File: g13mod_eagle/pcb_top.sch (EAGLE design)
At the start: 4 parts

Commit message: wiring
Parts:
- added CN6: (no value), pinhead-half-pitch:THROUHOLE18
- added CN7: (no value), pinhead-half-pitch:THROUHOLE15
- added JP2, JP3: (no value), pinhead-half-pitch:THROUHOLE05
- added JP4, JP7: (no value), pinhead-half-pitch:THROUHOLE04
- added JP5, JP6: (no value), pinhead-half-pitch:THROUHOLE12
- added LED1, LED2, LED3, LED4: (no value), led:LEDCHIPLED_1206
- added R1, R2, R3, R4: (no value), rcl:R-US_R0603
- renumbered S1 to M1, S2 to M2, S3 to M3, S4 to MR
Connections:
- new net CN6_1: CN6.1, M3.S1
- new net CN6_10: CN6.10, JP5.5
- new net CN6_11: CN6.11, JP5.6
- new net CN6_12: CN6.12, M1.S1
- new net CN6_13: CN6.13, JP5.7
- new net CN6_14: CN6.14, JP5.8
- new net CN6_15: CN6.15, JP5.9, M2.S1
- new net CN6_16: CN6.16, JP5.10
- new net CN6_17: CN6.17, JP5.11
- new net CN6_18: CN6.18, JP5.12
- new net CN6_2: CN6.2, MR.S1
- new net CN6_3: CN6.3, JP6.10
- new net CN6_4: CN6.4, JP6.11
- new net CN6_5: CN6.5, JP6.12
- new net CN6_6: CN6.6, JP5.1
- new net CN6_7: CN6.7, JP5.2
- new net CN6_8: CN6.8, JP5.3
- new net CN6_9: CN6.9, JP5.4
- new net CN7_1: CN7.1, JP2.1
- new net CN7_10: CN7.10, JP6.4
- new net CN7_11: CN7.11, JP6.5
- new net CN7_12: CN7.12, JP6.6
- new net CN7_13: CN7.13, JP6.7
- new net CN7_14: CN7.14, JP6.8
- new net CN7_15: CN7.15, JP6.9
- new net CN7_2: CN7.2, JP2.2
- new net CN7_3: CN7.3, JP2.3
- new net CN7_4: CN7.4, JP2.4
- new net CN7_5: CN7.5, M1.P1, M2.P1, MR.P1
- new net CN7_6: CN7.6, JP2.5
- new net CN7_7: CN7.7, JP6.1, M3.P1
- new net CN7_8: CN7.8, JP6.2
- new net CN7_9: CN7.9, JP6.3
- new net LED_M1: JP3.4, R1.1
- new net LED_M2: JP3.3, R2.1
- new net LED_M3: JP3.2, R3.1
- new net LED_MR: JP3.1, R4.1
- new net N$1: JP4.1, JP7.1
- new net N$2: JP4.2, JP7.2
- new net N$3: JP4.3, JP7.3
- new net N$4: JP4.4, JP7.4
- new net N$5: JP3.5, LED1.A, LED2.A, LED3.A, LED4.A
- new net N$6: LED1.C, R1.2
- new net N$7: LED2.C, R2.2
- new net N$8: LED3.C, R3.2
- new net N$9: LED4.C, R4.2

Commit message: wiring top pcb
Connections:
- net CN6_15: no longer JP5.9
- net CN6_16: now also JP5.9; no longer JP5.10
- net CN6_17: now also JP5.10; no longer JP5.11
- net CN6_18: now also JP5.11; no longer JP5.12
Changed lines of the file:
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@@
 </segment>
 <segment>
-<pinref part="JP5" gate="G$1" pin="12"/>
-<wire x1="-2.54" y1="0" x2="-2.54" y2="-5.08" width="0.1524" layer="91"/>
-<label x="-2.54" y="-5.08" size="1.778" layer="95" rot="R270" xref="yes"/>
+<label x="0" y="-5.08" size="1.778" layer="95" rot="R270" xref="yes"/>
+<pinref part="JP5" gate="G$1" pin="11"/>
+<wire x1="0" y1="0" x2="0" y2="-5.08" width="0.1524" layer="91"/>
 </segment>
 </net>
@@
 </segment>
 <segment>
-<label x="0" y="-5.08" size="1.778" layer="95" rot="R270" xref="yes"/>
-<pinref part="JP5" gate="G$1" pin="11"/>
-<wire x1="0" y1="0" x2="0" y2="-5.08" width="0.1524" layer="91"/>
+<label x="2.54" y="-5.08" size="1.778" layer="95" rot="R270" xref="yes"/>
+<pinref part="JP5" gate="G$1" pin="10"/>
+<wire x1="2.54" y1="0" x2="2.54" y2="-5.08" width="0.1524" layer="91"/>
 </segment>
 </net>
@@
 </segment>
 <segment>
-<label x="2.54" y="-5.08" size="1.778" layer="95" rot="R270" xref="yes"/>
-<pinref part="JP5" gate="G$1" pin="10"/>
-<wire x1="2.54" y1="0" x2="2.54" y2="-5.08" width="0.1524" layer="91"/>
+<label x="5.08" y="-5.08" size="1.778" layer="95" rot="R270" xref="yes"/>
+<pinref part="JP5" gate="G$1" pin="9"/>
+<wire x1="5.08" y1="0" x2="5.08" y2="-5.08" width="0.1524" layer="91"/>
 </segment>
 </net>
@@
 <label x="25.4" y="25.4" size="1.778" layer="95" xref="yes"/>
 </segment>
-<segment>
-<label x="5.08" y="-5.08" size="1.778" layer="95" rot="R270" xref="yes"/>
-<pinref part="JP5" gate="G$1" pin="9"/>
-<wire x1="5.08" y1="0" x2="5.08" y2="-5.08" width="0.1524" layer="91"/>
-</segment>
 </net>

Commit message: Edit connector
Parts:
- removed JP5, JP6: (no value), pinhead-half-pitch:THROUHOLE12
- added JP1: (no value), pinhead-half-pitch:THROUHOLE06
- added JP8: (no value), pinhead-half-pitch:THROUHOLE11
- JP2: device pinhead-half-pitch:THROUHOLE05 -> pinhead-half-pitch:THROUHOLE11
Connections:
- net CN6_10: now also JP8.5; no longer JP5.5
- net CN6_11: now also JP8.6; no longer JP5.6
- net CN6_13: now also JP8.7; no longer JP5.7
- net CN6_14: now also JP8.8; no longer JP5.8
- net CN6_16: now also JP8.9; no longer JP5.9
- net CN6_17: now also JP8.10; no longer JP5.10
- net CN6_18: now also JP8.11; no longer JP5.11
- net CN6_3: now also JP2.9; no longer JP6.10
- net CN6_4: now also JP2.10; no longer JP6.11
- net CN6_5: now also JP2.11; no longer JP6.12
- net CN6_6: now also JP8.1; no longer JP5.1
- net CN6_7: now also JP8.2; no longer JP5.2
- net CN6_8: now also JP8.3; no longer JP5.3
- net CN6_9: now also JP8.4; no longer JP5.4
- net CN7_1: now also JP1.1; no longer JP2.1
- net CN7_10: now also JP2.3; no longer JP6.4
- net CN7_11: now also JP2.4; no longer JP6.5
- net CN7_12: now also JP2.5; no longer JP6.6
- net CN7_13: now also JP2.6; no longer JP6.7
- net CN7_14: now also JP2.7; no longer JP6.8
- net CN7_15: now also JP2.8; no longer JP6.9
- net CN7_2: now also JP1.2; no longer JP2.2
- net CN7_3: now also JP1.3; no longer JP2.3
- net CN7_4: now also JP1.4; no longer JP2.4
- net CN7_6: now also JP1.5; no longer JP2.5
- net CN7_7: now also JP1.6; no longer JP6.1
- net CN7_8: now also JP2.1; no longer JP6.2
- net CN7_9: now also JP2.2; no longer JP6.3

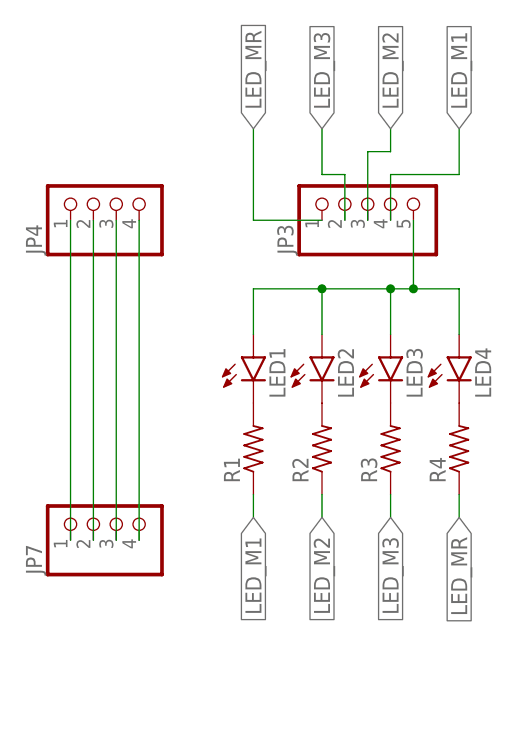
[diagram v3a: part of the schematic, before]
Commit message: wiring middle pcb
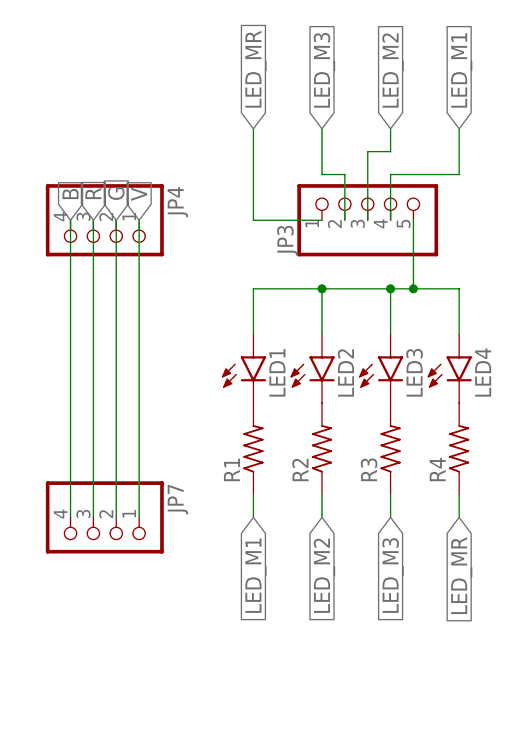
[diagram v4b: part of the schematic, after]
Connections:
- net N$1 renamed V
- net N$2 renamed G
- net N$3 renamed R
- net N$4 renamed B
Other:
- moved on the sheet: JP4, JP7
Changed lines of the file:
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@@
 <attribute name="VALUE" x="-12.7" y="34.29" size="1.778" layer="96" rot="R90"/>
 </instance>
-<instance part="JP4" gate="G$1" x="-50.8" y="40.64" smashed="yes" rot="R90">
-<attribute name="NAME" x="-59.055" y="34.29" size="1.778" layer="95" rot="R90"/>
-<attribute name="VALUE" x="-43.18" y="34.29" size="1.778" layer="96" rot="R90"/>
+<instance part="JP4" gate="G$1" x="-53.34" y="35.56" smashed="yes" rot="R270">
+<attribute name="NAME" x="-45.085" y="41.91" size="1.778" layer="95" rot="R270"/>
+<attribute name="VALUE" x="-60.96" y="41.91" size="1.778" layer="96" rot="R270"/>
 </instance>
-<instance part="JP7" gate="G$1" x="-50.8" y="5.08" smashed="yes" rot="R90">
-<attribute name="NAME" x="-59.055" y="-1.27" size="1.778" layer="95" rot="R90"/>
-<attribute name="VALUE" x="-43.18" y="-1.27" size="1.778" layer="96" rot="R90"/>
+<instance part="JP7" gate="G$1" x="-53.34" y="2.54" smashed="yes" rot="R270">
+<attribute name="NAME" x="-45.085" y="8.89" size="1.778" layer="95" rot="R270"/>
+<attribute name="VALUE" x="-60.96" y="8.89" size="1.778" layer="96" rot="R270"/>
 </instance>
 <instance part="LED1" gate="G$1" x="-35.56" y="22.86" smashed="yes">
@@
 </busses>
 <nets>
-<net name="N$1" class="0">
+<net name="V" class="0">
 <segment>
 <pinref part="JP4" gate="G$1" pin="1"/>
 <pinref part="JP7" gate="G$1" pin="1"/>
-<wire x1="-55.88" y1="38.1" x2="-55.88" y2="2.54" width="0.1524" layer="91"/>
+<wire x1="-48.26" y1="38.1" x2="-48.26" y2="5.08" width="0.1524" layer="91"/>
+<label x="-48.26" y="38.1" size="1.778" layer="95" rot="R90" xref="yes"/>
 </segment>
 </net>
-<net name="N$2" class="0">
+<net name="G" class="0">
 <segment>
 <pinref part="JP4" gate="G$1" pin="2"/>
 <pinref part="JP7" gate="G$1" pin="2"/>
-<wire x1="-53.34" y1="38.1" x2="-53.34" y2="2.54" width="0.1524" layer="91"/>
+<wire x1="-50.8" y1="38.1" x2="-50.8" y2="5.08" width="0.1524" layer="91"/>
+<label x="-50.8" y="38.1" size="1.778" layer="95" rot="R90" xref="yes"/>
 </segment>
 </net>
-<net name="N$3" class="0">
+<net name="R" class="0">
 <segment>
 <pinref part="JP4" gate="G$1" pin="3"/>
 <pinref part="JP7" gate="G$1" pin="3"/>
-<wire x1="-50.8" y1="38.1" x2="-50.8" y2="2.54" width="0.1524" layer="91"/>
+<wire x1="-53.34" y1="38.1" x2="-53.34" y2="5.08" width="0.1524" layer="91"/>
+<label x="-53.34" y="38.1" size="1.778" layer="95" rot="R90" xref="yes"/>
 </segment>
 </net>
-<net name="N$4" class="0">
+<net name="B" class="0">
 <segment>
 <pinref part="JP4" gate="G$1" pin="4"/>
 <pinref part="JP7" gate="G$1" pin="4"/>
-<wire x1="-48.26" y1="38.1" x2="-48.26" y2="2.54" width="0.1524" layer="91"/>
+<wire x1="-55.88" y1="38.1" x2="-55.88" y2="5.08" width="0.1524" layer="91"/>
+<label x="-55.88" y="38.1" size="1.778" layer="95" rot="R90" xref="yes"/>
 </segment>
 </net>

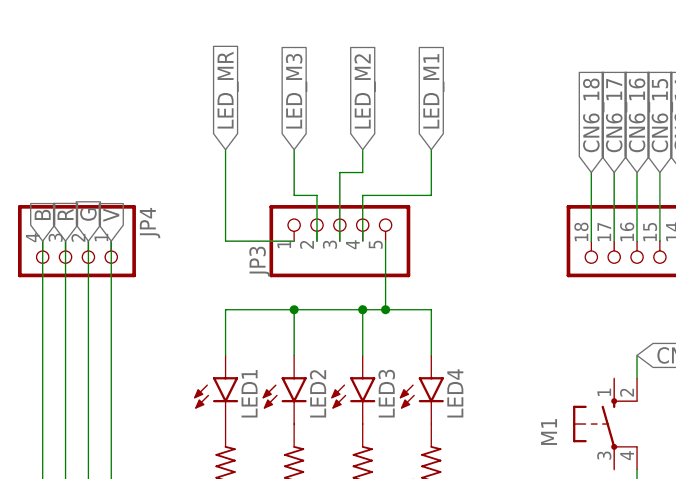
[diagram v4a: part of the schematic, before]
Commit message: Fix LED color
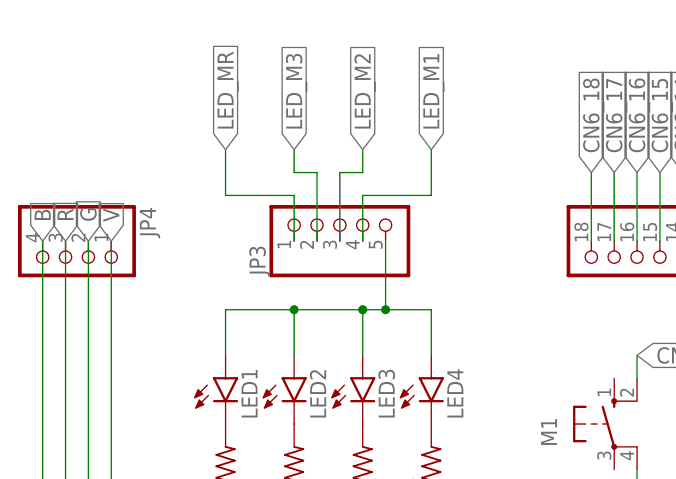
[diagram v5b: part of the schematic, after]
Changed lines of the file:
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@@
 <segment>
 <pinref part="JP3" gate="G$1" pin="2"/>
-<wire x1="-25.4" y1="38.1" x2="-25.4" y2="43.18" width="0.1524" layer="91"/>
-<wire x1="-25.4" y1="43.18" x2="-27.94" y2="43.18" width="0.1524" layer="91"/>
-<wire x1="-27.94" y1="43.18" x2="-27.94" y2="48.26" width="0.1524" layer="91"/>
+<wire x1="-25.4" y1="38.1" x2="-25.4" y2="45.72" width="0.1524" layer="91"/>
+<wire x1="-25.4" y1="45.72" x2="-27.94" y2="45.72" width="0.1524" layer="91"/>
+<wire x1="-27.94" y1="45.72" x2="-27.94" y2="48.26" width="0.1524" layer="91"/>
 <label x="-27.94" y="48.26" size="1.778" layer="95" rot="R90" xref="yes"/>
 </segment>
@@
 <segment>
 <pinref part="JP3" gate="G$1" pin="1"/>
-<wire x1="-27.94" y1="38.1" x2="-35.56" y2="38.1" width="0.1524" layer="91"/>
-<wire x1="-35.56" y1="38.1" x2="-35.56" y2="48.26" width="0.1524" layer="91"/>
+<wire x1="-27.94" y1="38.1" x2="-27.94" y2="43.18" width="0.1524" layer="91"/>
+<wire x1="-27.94" y1="43.18" x2="-35.56" y2="43.18" width="0.1524" layer="91"/>
+<wire x1="-35.56" y1="43.18" x2="-35.56" y2="48.26" width="0.1524" layer="91"/>
 <label x="-35.56" y="48.26" size="1.778" layer="95" rot="R90" xref="yes"/>
 </segment>
